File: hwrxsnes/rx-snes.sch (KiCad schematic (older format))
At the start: 20 parts, among them IC1 ATMEGA328-A, P1 +5v, P2 Clock, P3 Latch, P4 Data, P5 GND, P6 nRF, P7 ISP, P8 RX, P9 TX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

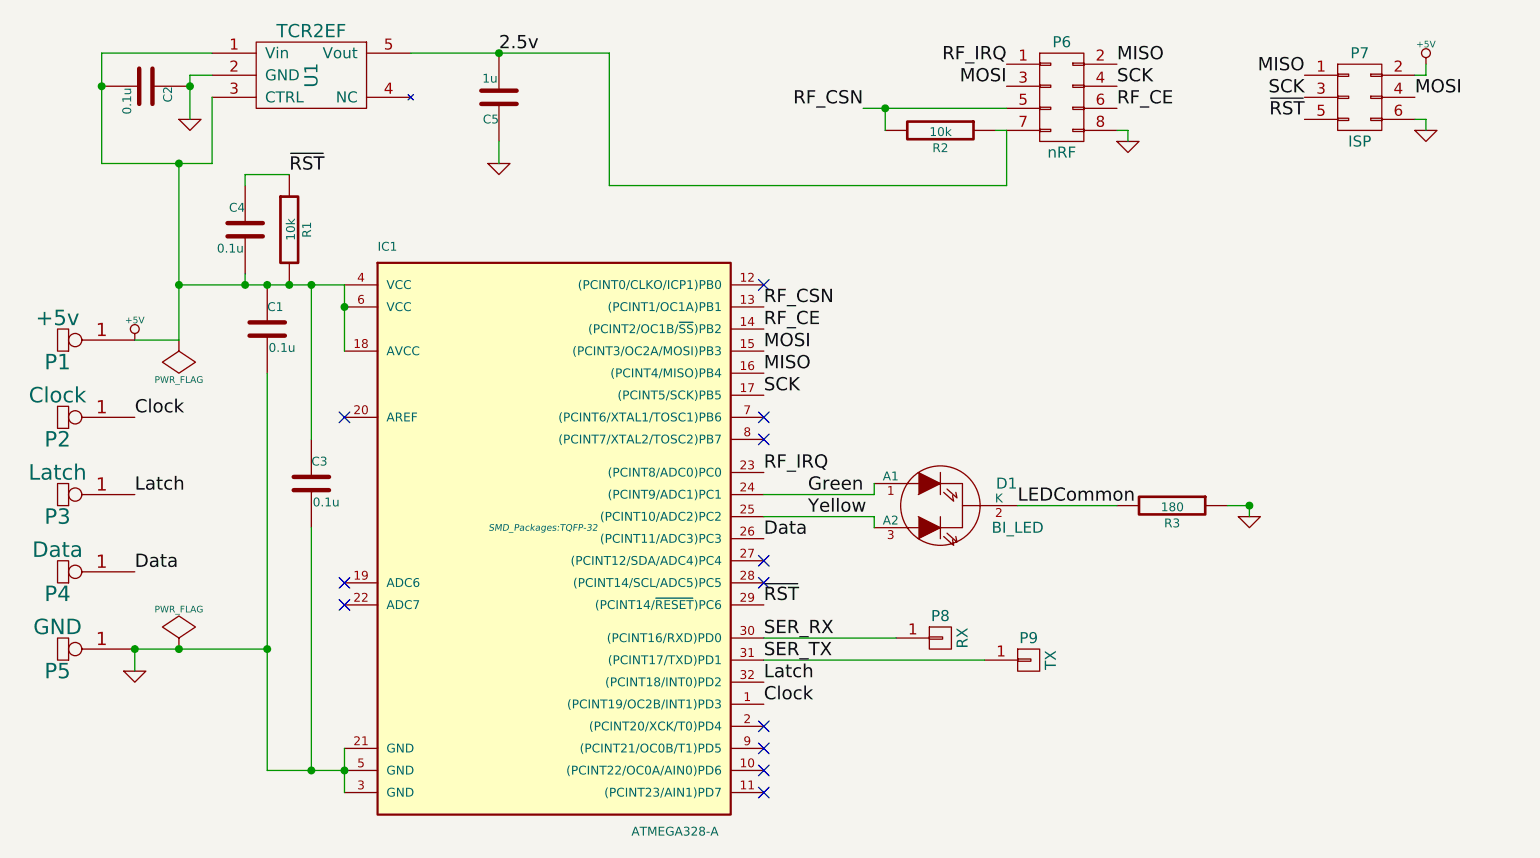
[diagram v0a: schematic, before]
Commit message: Reroute the SNES RX board.
Both to add a 16MHz crystal and align the holes for easier wiring.

Refs #2
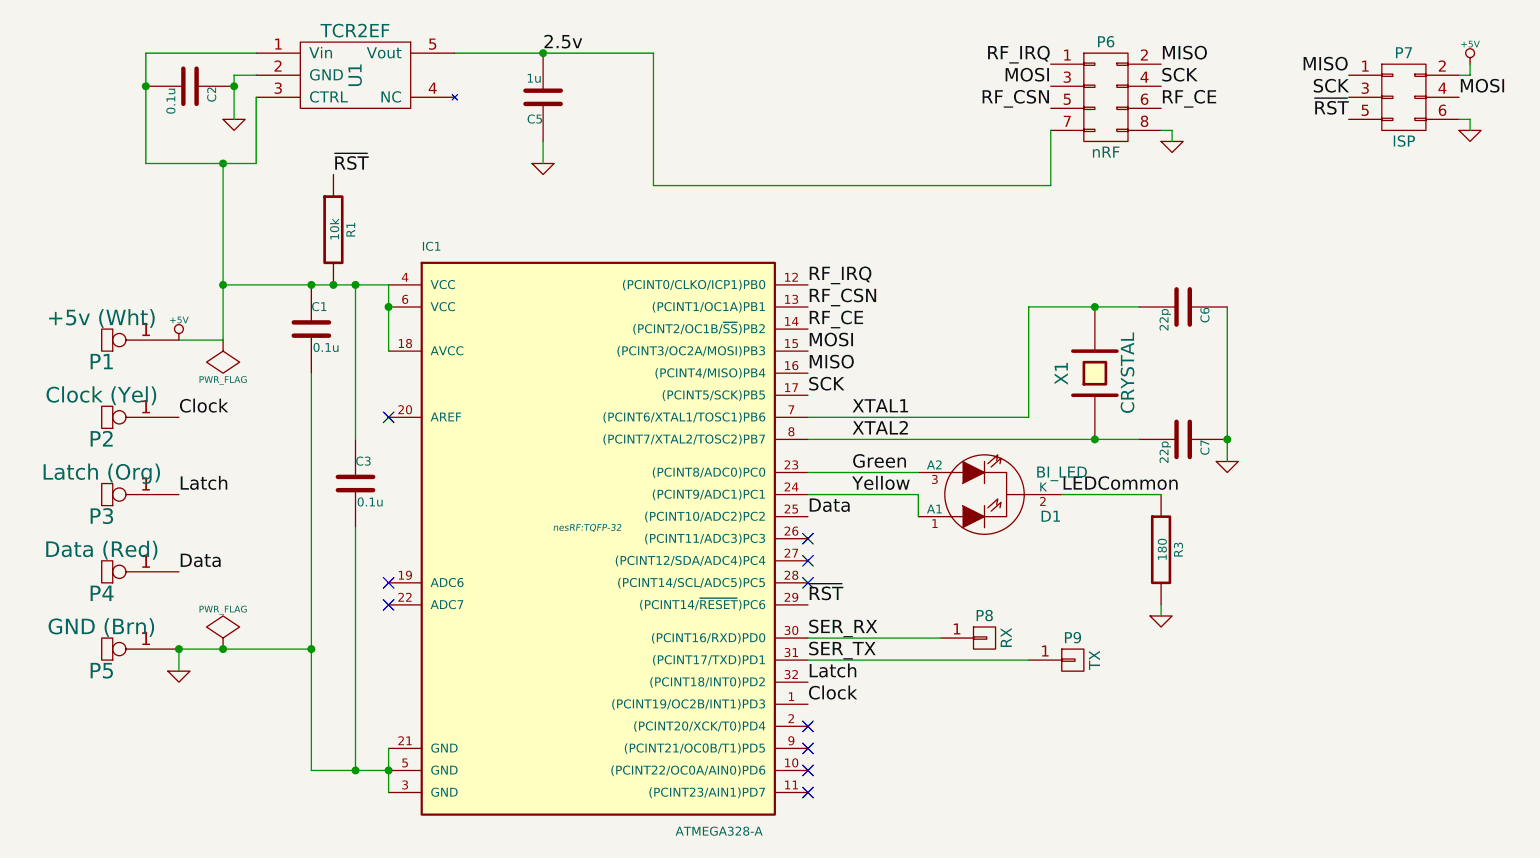
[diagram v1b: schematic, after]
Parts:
- removed C4: 0.1u, SMD_Packages:SMD-0402_c, symbol C
- removed R2: 10k, SMD_Packages:SMD-0402_r, symbol R
- added C6, C7: 22p, Capacitors_SMD:C_0402, symbol C
- added X1: CRYSTAL, nesRF:TSX-3225, symbol CRYSTAL
- C1, C2, C3, C5: footprint SMD_Packages:SMD-0402_c -> Capacitors_SMD:C_0402
- IC1: footprint SMD_Packages:TQFP-32 -> nesRF:TQFP-32
- P1: value +5v -> +5v (Wht)
- P2: value Clock -> Clock (Yel)
- P3: value Latch -> Latch (Org)
- P4: value Data -> Data (Red)
- P5: value GND -> GND (Brn)
- P7: footprint Pin_Headers:Pin_Header_Straight_2x03 -> nesRF:ISP_POGO
- R1, R3: footprint SMD_Packages:SMD-0402_r -> Resistors_SMD:R_0402
- U1: footprint SMD_Packages:SOT-23-5 -> nesRF:SOT23-5
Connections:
- net Data: now also IC1.25 ((PCINT10/ADC2)PC2); no longer IC1.26 ((PCINT11/ADC3)PC3)
- net GND: now also R3.2, C6.1, C7.1; no longer R3.1
- net Green: now also D1.3 (A2), IC1.23 ((PCINT8/ADC0)PC0); no longer D1.1 (A1), IC1.24 ((PCINT9/ADC1)PC1)
- net LEDCommon: now also R3.1; no longer R3.2
- net RF_IRQ: now also IC1.12 ((PCINT0/CLKO/ICP1)PB0); no longer IC1.23 ((PCINT8/ADC0)PC0)
- net Yellow: now also D1.1 (A1), IC1.24 ((PCINT9/ADC1)PC1); no longer D1.3 (A2), IC1.25 ((PCINT10/ADC2)PC2)
- net XTAL1: now reaches IC1.7 ((PCINT6/XTAL1/TOSC1)PB6)
- net XTAL1: now also C6.2, X1.2
- net XTAL2: now reaches IC1.8 ((PCINT7/XTAL2/TOSC2)PB7)
- net XTAL2: now also C7.2, X1.1
- no-connect marks 12 -> 10
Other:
- moved on the sheet: C1, C2, C3, C5, D1, IC1, P1, P2, P3, P4, P5, P6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
